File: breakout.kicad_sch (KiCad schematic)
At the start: 9 parts, among them J1 Conn_01x09_Socket, U11 HV5622PG, U12 HV5622PG

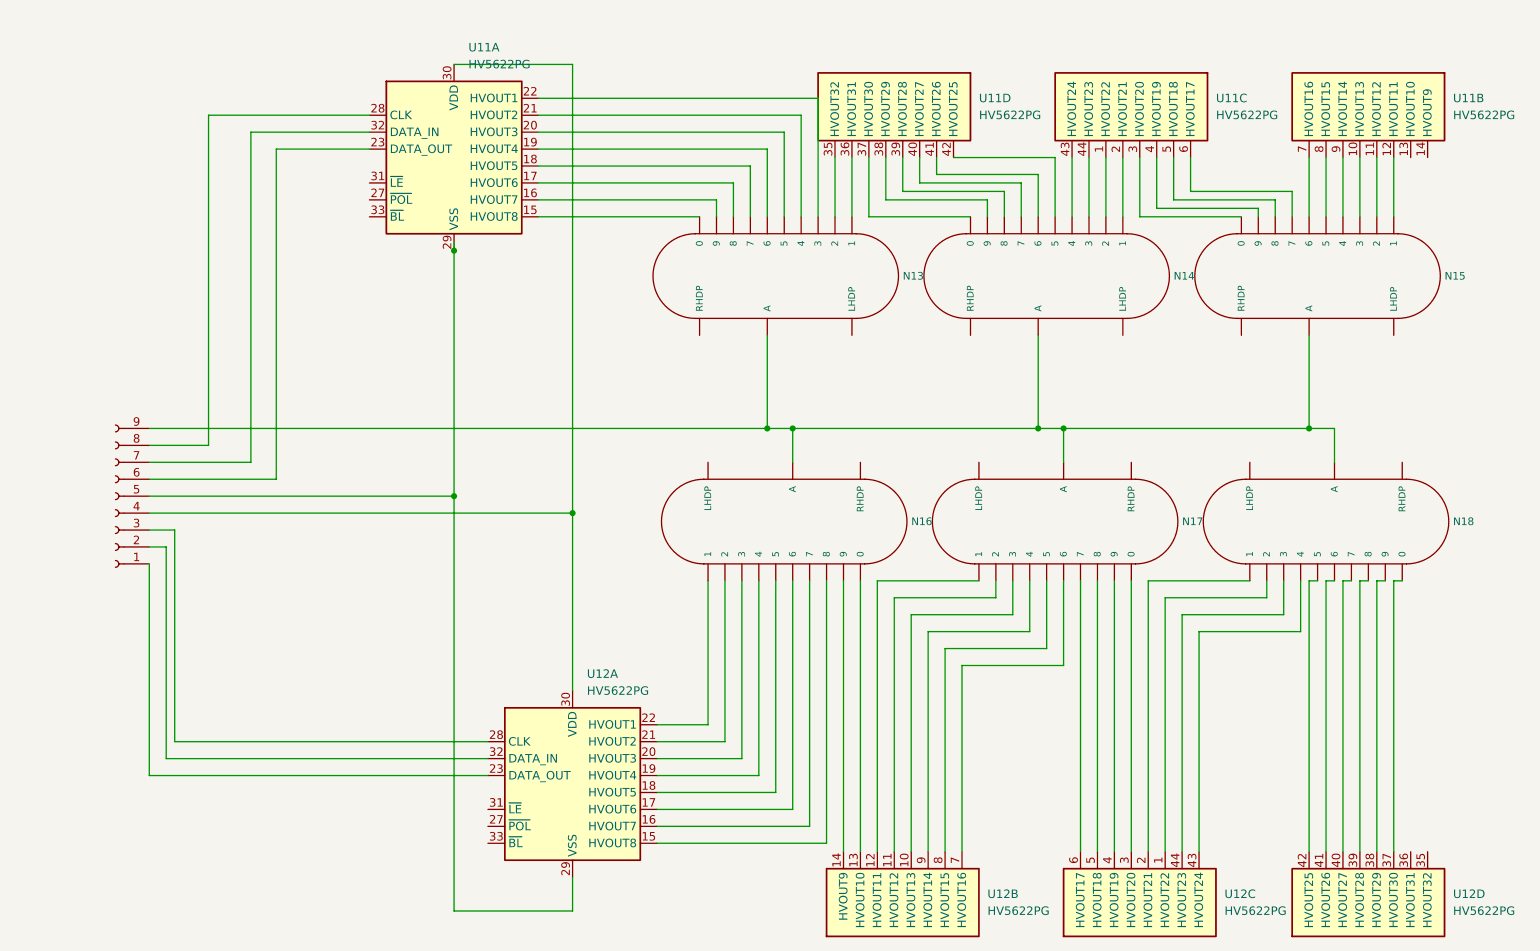
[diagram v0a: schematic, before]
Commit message: improve boost converter design and move to net labels
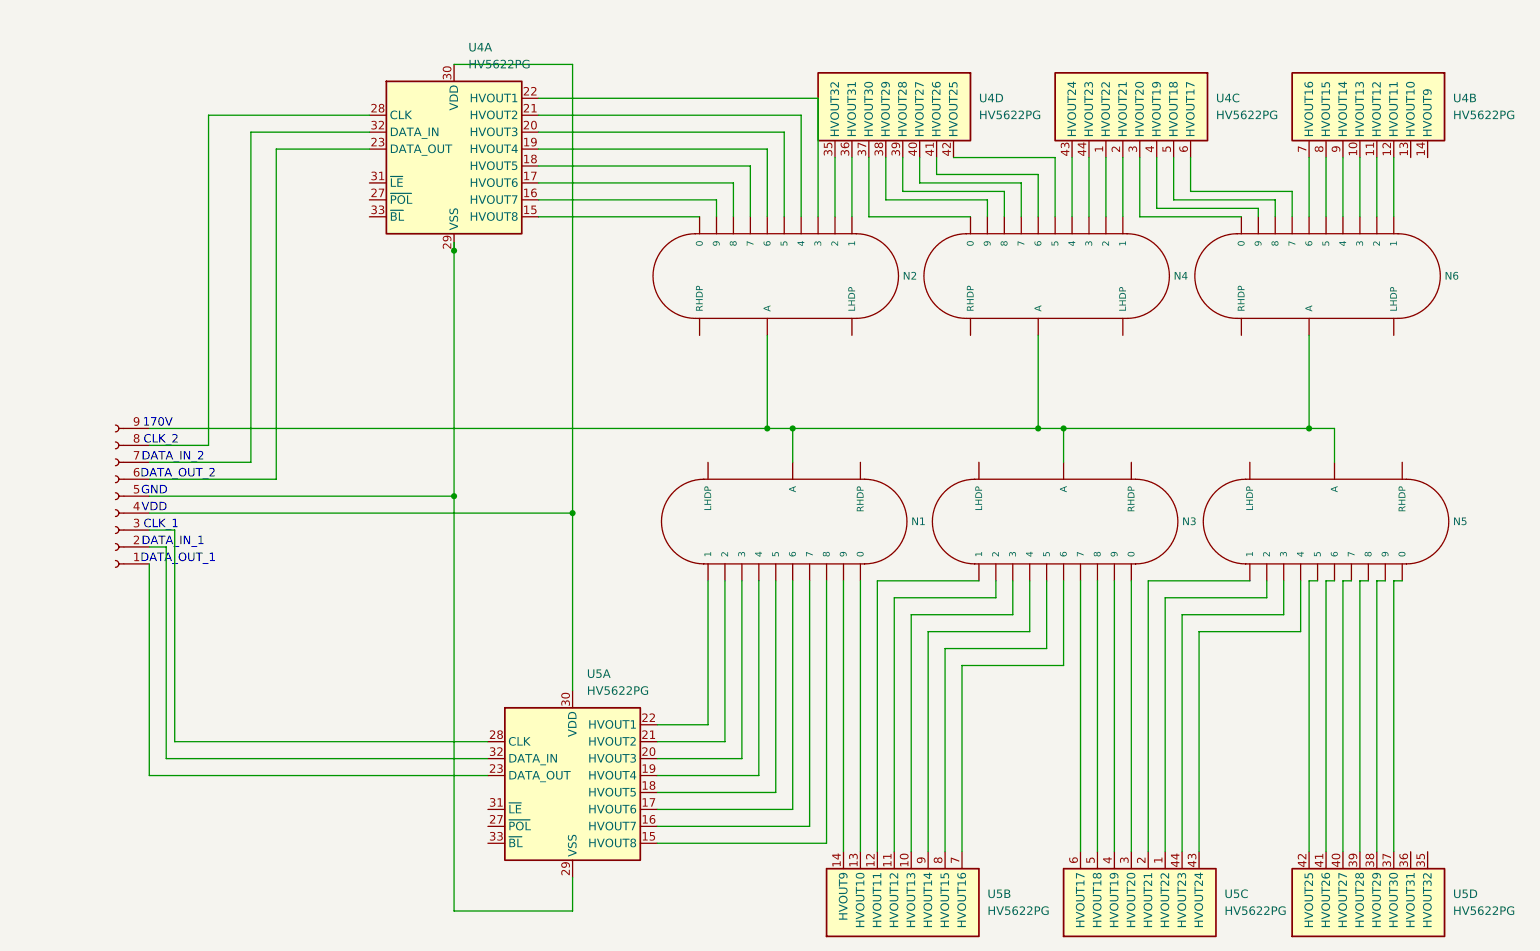
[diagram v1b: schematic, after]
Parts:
- renumbered J1 to J2, N16 to N1, N13 to N2, N17 to N3, N14 to N4, N18 to N5, N15 to N6, U11 to U4, U12 to U5
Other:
- note added: "170V"
- note added: "CLK_1"
- note added: "CLK_2"
- note added: "DATA_IN_1"
- note added: "DATA_IN_2"
- note added: "DATA_OUT_1"
- note added: "DATA_OUT_2"
- note added: "GND"
- note added: "VDD"
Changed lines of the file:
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@@
 	(generator_version "10.0")
 	(paper "A4")
+	(text "DATA_IN_2"
+		(exclude_from_sim yes)
+		(at 69.596 89.408 0)
+		(effects
+			(font
+				(size 1.27 1.27)
+			)
+		)
+	)
+	(text "CLK_2"
+		(exclude_from_sim yes)
+		(at 67.818 86.868 0)
+		(effects
+			(font
+				(size 1.27 1.27)
+			)
+		)
+	)
+	(text "CLK_1"
+		(exclude_from_sim yes)
+		(at 67.818 99.568 0)
+		(effects
+			(font
+				(size 1.27 1.27)
+			)
+		)
+	)
+	(text "VDD"
+		(exclude_from_sim yes)
+		(at 66.802 97.028 0)
+		(effects
+			(font
+				(size 1.27 1.27)
+			)
+		)
+	)
+	(text "DATA_OUT_1"
+		(exclude_from_sim yes)
+		(at 70.358 104.648 0)
+		(effects
+			(font
+				(size 1.27 1.27)
+			)
+		)
+	)
+	(text "DATA_OUT_2"
+		(exclude_from_sim yes)
+		(at 70.358 91.948 0)
+		(effects
+			(font
+				(size 1.27 1.27)
+			)
+		)
+	)
+	(text "GND"
+		(exclude_from_sim yes)
+		(at 66.802 94.488 0)
+		(effects
+			(font
+				(size 1.27 1.27)
+			)
+		)
+	)
+	(text "170V"
+		(exclude_from_sim yes)
+		(at 67.31 84.328 0)
+		(effects
+			(font
+				(size 1.27 1.27)
+			)
+		)
+	)
+	(text "DATA_IN_1"
+		(exclude_from_sim yes)
+		(at 69.596 102.108 0)
+		(effects
+			(font
+				(size 1.27 1.27)
+			)
+		)
+	)
 	(junction
 		(at 240.03 85.09)
@@
 		(dnp no)
 		(fields_autoplaced yes)
-		(property "Reference" "U11"
+		(property "Reference" "U4"
 			(at 190.5 35.5599 90)
 			(show_name no)
@@
 			(project "nixie"
 				(path "/002ab559-5526-44bb-90c7-ab66e50376b8"
-					(reference "U11")
+					(reference "U4")
 					(unit 4)
 				)
@@
 		(dnp no)
 		(fields_autoplaced yes)
-		(property "Reference" "N16"
+		(property "Reference" "N1"
 			(at 180.34 99.06 90)
 			(show_name no)
@@
 			(project "nixie"
 				(path "/002ab559-5526-44bb-90c7-ab66e50376b8"
-					(reference "N16")
+					(reference "N1")
 					(unit 1)
 				)
@@
 		(dnp no)
 		(fields_autoplaced yes)
-		(property "Reference" "U12"
+		(property "Reference" "U5"
 			(at 131.6833 121.92 0)
 			(show_name no)
@@
 			(project "nixie"
 				(path "/002ab559-5526-44bb-90c7-ab66e50376b8"
-					(reference "U12")
+					(reference "U5")
 					(unit 1)
 				)
@@
 		(dnp no)
 		(fields_autoplaced yes)
-		(property "Reference" "N18"
+		(property "Reference" "N5"
 			(at 261.62 99.06 90)
 			(show_name no)
@@
 			(project "nixie"
 				(path "/002ab559-5526-44bb-90c7-ab66e50376b8"
-					(reference "N18")
+					(reference "N5")
 					(unit 1)
 				)
@@
 		(dnp no)
 		(fields_autoplaced yes)
-		(property "Reference" "U12"
+		(property "Reference" "U5"
 			(at 227.33 154.9399 90)
 			(show_name no)
@@
 			(project "nixie"
 				(path "/002ab559-5526-44bb-90c7-ab66e50376b8"
-					(reference "U12")
+					(reference "U5")
 					(unit 3)
 				)
@@
 		(dnp no)
 		(fields_autoplaced yes)
-		(property "Reference" "N14"
+		(property "Reference" "N4"
 			(at 219.71 62.23 90)
 			(show_name no)
@@
 			(project "nixie"
 				(path "/002ab559-5526-44bb-90c7-ab66e50376b8"
-					(reference "N14")
+					(reference "N4")
 					(unit 1)
 				)
@@
 		(dnp no)
 		(fields_autoplaced yes)
-		(property "Reference" "N17"
+		(property "Reference" "N3"
 			(at 220.98 99.06 90)
 			(show_name no)
@@
 			(project "nixie"
 				(path "/002ab559-5526-44bb-90c7-ab66e50376b8"
-					(reference "N17")
+					(reference "N3")
 					(unit 1)
 				)
@@
 		(dnp no)
 		(fields_autoplaced yes)
-		(property "Reference" "N15"
+		(property "Reference" "N6"
 			(at 260.35 62.23 90)
 			(show_name no)
@@
 			(project "nixie"
 				(path "/002ab559-5526-44bb-90c7-ab66e50376b8"
-					(reference "N15")
+					(reference "N6")
 					(unit 1)
 				)
@@
 		(dnp no)
 		(fields_autoplaced yes)
-		(property "Reference" "U11"
+		(property "Reference" "U4"
 			(at 261.62 35.5599 90)
 			(show_name no)
@@
 			(project "nixie"
 				(path "/002ab559-5526-44bb-90c7-ab66e50376b8"
-					(reference "U11")
+					(reference "U4")
 					(unit 2)
 				)
@@
 		(dnp no)
 		(fields_autoplaced yes)
-		(property "Reference" "U11"
+		(property "Reference" "U4"
 			(at 226.06 35.5599 90)
 			(show_name no)
@@
 			(project "nixie"
 				(path "/002ab559-5526-44bb-90c7-ab66e50376b8"
-					(reference "U11")
+					(reference "U4")
 					(unit 3)
 				)
@@
 		(dnp no)
 		(fields_autoplaced yes)
-		(property "Reference" "J1"
+		(property "Reference" "J2"
 			(at 59.69 96.5201 0)
 			(hide yes)
@@
 			(project "nixie"
 				(path "/002ab559-5526-44bb-90c7-ab66e50376b8"
-					(reference "J1")
+					(reference "J2")
 					(unit 1)
 				)
@@
 		(dnp no)
 		(fields_autoplaced yes)
-		(property "Reference" "U12"
+		(property "Reference" "U5"
 			(at 261.62 154.9399 90)
 			(show_name no)
@@
 			(project "nixie"
 				(path "/002ab559-5526-44bb-90c7-ab66e50376b8"
-					(reference "U12")
+					(reference "U5")
 					(unit 4)
 				)
@@
 		(dnp no)
 		(fields_autoplaced yes)
-		(property "Reference" "U11"
+		(property "Reference" "U4"
 			(at 113.9033 27.94 0)
 			(show_name no)
@@
 			(project "nixie"
 				(path "/002ab559-5526-44bb-90c7-ab66e50376b8"
-					(reference "U11")
+					(reference "U4")
 					(unit 1)
 				)
@@
 		(dnp no)
 		(fields_autoplaced yes)
-		(property "Reference" "N13"
+		(property "Reference" "N2"
 			(at 179.07 62.23 90)
 			(show_name no)
@@
 			(project "nixie"
 				(path "/002ab559-5526-44bb-90c7-ab66e50376b8"
-					(reference "N13")
+					(reference "N2")
 					(unit 1)
 				)
@@
 		(dnp no)
 		(fields_autoplaced yes)
-		(property "Reference" "U12"
+		(property "Reference" "U5"
 			(at 191.77 154.9399 90)
 			(show_name no)
@@
 			(project "nixie"
 				(path "/002ab559-5526-44bb-90c7-ab66e50376b8"
-					(reference "U12")
+					(reference "U5")
 					(unit 2)
 				)
@@
 	(sheet_instances
 		(path "/"
-			(page "3")
+			(page "2")
 		)
 	)

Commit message: add usb c pd deceiver footprint
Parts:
- J2: footprint (none) -> Connector_PinSocket_2.54mm:PinSocket_1x09_P2.54mm_Vertical
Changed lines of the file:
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@@
 			)
 		)
-		(property "Footprint" ""
+		(property "Footprint" "Connector_PinSocket_2.54mm:PinSocket_1x09_P2.54mm_Vertical"
 			(at 60.96 95.25 0)
 			(hide yes)
